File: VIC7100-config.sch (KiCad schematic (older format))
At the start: 42 parts, among them J1 TAG-10PIN, Q1 DMG1013UWQ-7, U13 VIC7100, U2 GD25LQ256DWIGR, U7 STM811RW16F, Y2 ABM8G-25.000MHZ-18-D2Y-T, Y3 ABM8G-27.000MHZ-18-D2Y-T

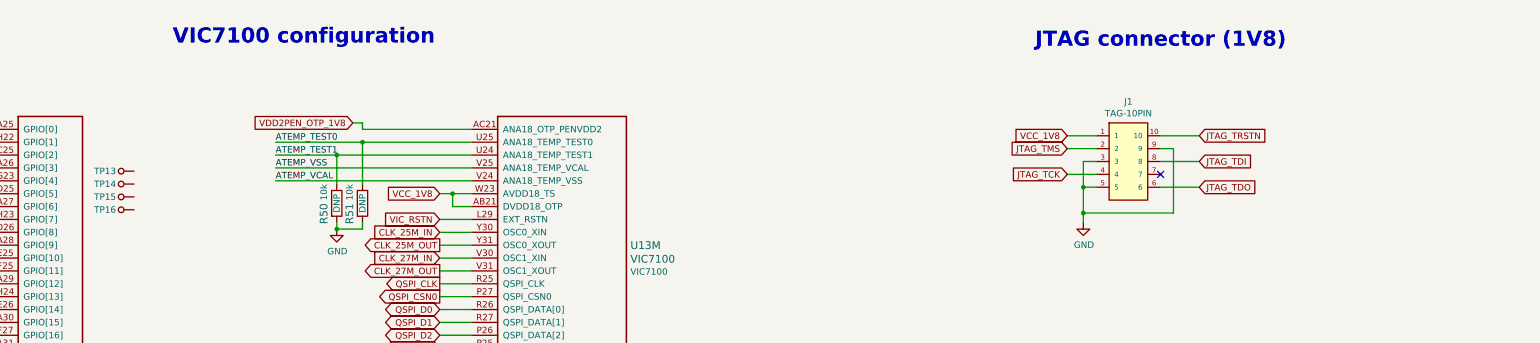
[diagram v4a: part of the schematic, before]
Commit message: Added UART3 testpoints
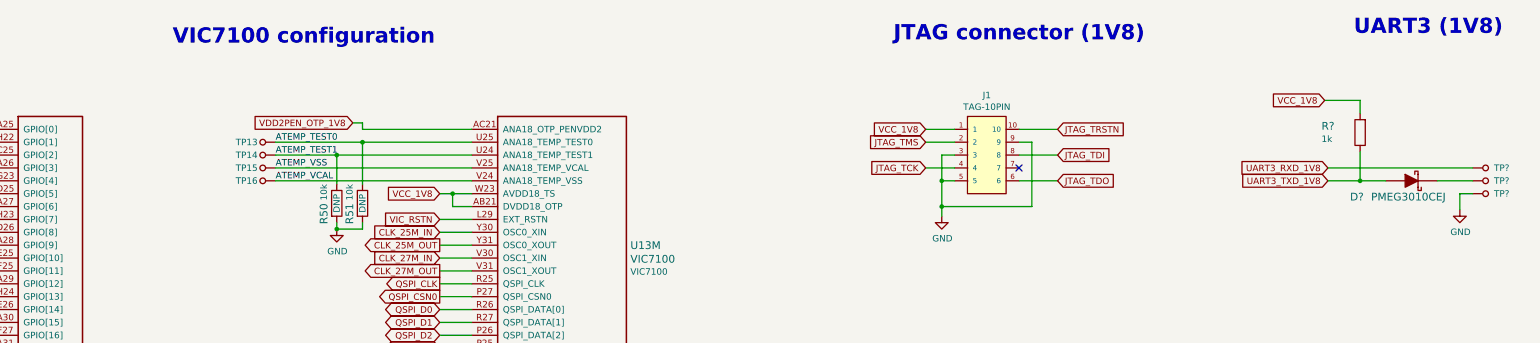
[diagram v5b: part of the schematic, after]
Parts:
- added D?: PMEG3010CEJ, arvsom-footprints:SOD-323F, symbol arvsom:PMEG3010CEJ
- added R?: R_1k_0402, arvsom-footprints:0402-res, symbol arvsom:R_1k_0402
- added TP? (x3): TP_SMD_0_75MM, arvsom-footprints:Testpoint_smd_0_75mm, symbol arvsom:TP_SMD_0_75MM
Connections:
- net ATEMP_TEST0: now also TP13.1
- net ATEMP_TEST1: now also TP14.1
- net ATEMP_VCAL: now also TP16.1
- net ATEMP_VSS: now also TP15.1
- net GND: now also TP?.1
- net UART3_RXD_1V8: now also TP?.1
- net UART3_TXD_1V8: now also D?.A, R?.1
- net VCC_1V8: now also R?.2
- new net: D?.K, TP?.1
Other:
- note added: "UART3 (1V8)"
- moved on the sheet: J1, TP13, TP14, TP15, TP16
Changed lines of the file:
@@
 L arvsom:TP_SMD_0_75MM TP13
 U 1 1 6275FE96
-P 3675 2575
-F 0 "TP13" V 3675 2450 50  0000 C CNN
-F 1 "TP_SMD_0_75MM" H 3675 2475 50  0001 C CNN
-F 2 "arvsom-footprints:Testpoint_smd_0_75mm" H 3875 2775 60  0001 L CNN
-F 3 "" H 3875 2875 60  0001 L CNN
-	1    3675 2575
+P 4775 2350
+F 0 "TP13" V 4775 2225 50  0000 C CNN
+F 1 "TP_SMD_0_75MM" H 4775 2250 50  0001 C CNN
+F 2 "arvsom-footprints:Testpoint_smd_0_75mm" H 4975 2550 60  0001 L CNN
+F 3 "" H 4975 2650 60  0001 L CNN
+	1    4775 2350
 	0    1    1    0
 $EndComp
@@
 L arvsom:TP_SMD_0_75MM TP14
 U 1 1 62760FCD
-P 3675 2675
-F 0 "TP14" V 3675 2550 50  0000 C CNN
-F 1 "TP_SMD_0_75MM" H 3675 2575 50  0001 C CNN
-F 2 "arvsom-footprints:Testpoint_smd_0_75mm" H 3875 2875 60  0001 L CNN
-F 3 "" H 3875 2975 60  0001 L CNN
-	1    3675 2675
+P 4775 2450
+F 0 "TP14" V 4775 2325 50  0000 C CNN
+F 1 "TP_SMD_0_75MM" H 4775 2350 50  0001 C CNN
+F 2 "arvsom-footprints:Testpoint_smd_0_75mm" H 4975 2650 60  0001 L CNN
+F 3 "" H 4975 2750 60  0001 L CNN
+	1    4775 2450
 	0    1    1    0
 $EndComp
@@
 L arvsom:TP_SMD_0_75MM TP15
 U 1 1 62761E35
-P 3675 2775
-F 0 "TP15" V 3675 2650 50  0000 C CNN
-F 1 "TP_SMD_0_75MM" H 3675 2675 50  0001 C CNN
-F 2 "arvsom-footprints:Testpoint_smd_0_75mm" H 3875 2975 60  0001 L CNN
-F 3 "" H 3875 3075 60  0001 L CNN
-	1    3675 2775
+P 4775 2550
+F 0 "TP15" V 4775 2425 50  0000 C CNN
+F 1 "TP_SMD_0_75MM" H 4775 2450 50  0001 C CNN
+F 2 "arvsom-footprints:Testpoint_smd_0_75mm" H 4975 2750 60  0001 L CNN
+F 3 "" H 4975 2850 60  0001 L CNN
+	1    4775 2550
 	0    1    1    0
 $EndComp
@@
 L arvsom:TP_SMD_0_75MM TP16
 U 1 1 62762BE9
-P 3675 2875
-F 0 "TP16" V 3675 2750 50  0000 C CNN
-F 1 "TP_SMD_0_75MM" H 3675 2775 50  0001 C CNN
-F 2 "arvsom-footprints:Testpoint_smd_0_75mm" H 3875 3075 60  0001 L CNN
-F 3 "" H 3875 3175 60  0001 L CNN
-	1    3675 2875
+P 4775 2650
+F 0 "TP16" V 4775 2525 50  0000 C CNN
+F 1 "TP_SMD_0_75MM" H 4775 2550 50  0001 C CNN
+F 2 "arvsom-footprints:Testpoint_smd_0_75mm" H 4975 2850 60  0001 L CNN
+F 3 "" H 4975 2950 60  0001 L CNN
+	1    4775 2650
 	0    1    1    0
 $EndComp
@@
 Text Notes 10975 7500 0    118  ~ 24
 Clock crystals
-Text Notes 10775 1625 0    118  ~ 24
+Text Notes 9675 1575 0    118  ~ 24
 JTAG connector (1V8)
 $Comp
@@
 L arvsom:TAG-10PIN J1
 U 1 1 6099DDAA
-P 11500 2500
-F 0 "J1" H 11500 2965 50  0000 C CNN
-F 1 "TAG-10PIN" H 11500 2874 50  0000 C CNN
-F 2 "arvsom-footprints:Tag-Connect_TC2050-IDC-NL" H 11250 2500 50  0001 L BNN
-F 3 "" H 11500 2500 50  0001 L BNN
-	1    11500 2500
+P 10400 2450
+F 0 "J1" H 10400 2915 50  0000 C CNN
+F 1 "TAG-10PIN" H 10400 2824 50  0000 C CNN
+F 2 "arvsom-footprints:Tag-Connect_TC2050-IDC-NL" H 10150 2450 50  0001 L BNN
+F 3 "" H 10400 2450 50  0001 L BNN
+	1    10400 2450
 	1    0    0    -1
 $EndComp
@@
 Text Notes 5875 5000 0    118  ~ 24
 VIC reset
-Text GLabel 12050 2700 2    50   Input ~ 0
+Text GLabel 10950 2650 2    50   Input ~ 0
 JTAG_TDO
-Text GLabel 11025 2600 0    50   Input ~ 0
+Text GLabel 9925 2550 0    50   Input ~ 0
 JTAG_TCK
-Text GLabel 12050 2500 2    50   Input ~ 0
+Text GLabel 10950 2450 2    50   Input ~ 0
 JTAG_TDI
-Text GLabel 11025 2400 0    50   Input ~ 0
+Text GLabel 9925 2350 0    50   Input ~ 0
 JTAG_TMS
-Text GLabel 12050 2300 2    50   Input ~ 0
+Text GLabel 10950 2250 2    50   Input ~ 0
 JTAG_TRSTN
-Text GLabel 11025 2300 0    50   Input ~ 0
+Text GLabel 9925 2250 0    50   Input ~ 0
 VCC_1V8
 Wire Wire Line
-	11250 2500 11150 2500
-Wire Wire Line
-	11150 2500 11150 2700
-Wire Wire Line
-	11750 2400 11850 2400
-Wire Wire Line
-	11850 2400 11850 2900
-Wire Wire Line
-	11850 2900 11150 2900
-Connection ~ 11150 2900
-Wire Wire Line
-	11150 2900 11150 2975
-NoConn ~ 11750 2600
+	10150 2450 10050 2450
+Wire Wire Line
+	10050 2450 10050 2650
+Wire Wire Line
+	10650 2350 10750 2350
+Wire Wire Line
+	10750 2350 10750 2850
+Wire Wire Line
+	10750 2850 10050 2850
+Connection ~ 10050 2850
+Wire Wire Line
+	10050 2850 10050 2925
+NoConn ~ 10650 2550
 $Comp
 L arvsom:GND #PWR?
 U 1 1 60A2B262
-P 11150 2975
+P 10050 2925
 AR Path="/607858CA/60A2B262" Ref="#PWR?"  Part="1"
 AR Path="/60805CC6/60A2B262" Ref="#PWR0212"  Part="1"
-F 0 "#PWR0212" H 11150 2725 50  0001 C CNN
-F 1 "GND" H 11155 2802 50  0000 C CNN
-F 2 "" H 11150 2975 50  0001 C CNN
-F 3 "" H 11150 2975 50  0001 C CNN
-	1    11150 2975
-	1    0    0    -1
-$EndComp
-Wire Wire Line
-	12050 2700 11750 2700
-Wire Wire Line
-	11750 2500 12050 2500
-Wire Wire Line
-	11750 2300 12050 2300
-Wire Wire Line
-	11025 2300 11250 2300
-Wire Wire Line
-	11025 2400 11250 2400
-Wire Wire Line
-	11025 2600 11250 2600
-Wire Wire Line
-	11250 2700 11150 2700
-Connection ~ 11150 2700
-Wire Wire Line
-	11150 2700 11150 2900
+F 0 "#PWR0212" H 10050 2675 50  0001 C CNN
+F 1 "GND" H 10055 2752 50  0000 C CNN
+F 2 "" H 10050 2925 50  0001 C CNN
+F 3 "" H 10050 2925 50  0001 C CNN
+	1    10050 2925
+	1    0    0    -1
+$EndComp
+Wire Wire Line
+	10950 2650 10650 2650
+Wire Wire Line
+	10650 2450 10950 2450
+Wire Wire Line
+	10650 2250 10950 2250
+Wire Wire Line
+	9925 2250 10150 2250
+Wire Wire Line
+	9925 2350 10150 2350
+Wire Wire Line
+	9925 2550 10150 2550
+Wire Wire Line
+	10150 2650 10050 2650
+Connection ~ 10050 2650
+Wire Wire Line
+	10050 2650 10050 2850
 Wire Wire Line
 	10225 6125 10150 6125
@@
 	1    0    0    -1
 $EndComp
+Text GLabel 13050 2550 0    50   Input ~ 0
+UART3_RXD_1V8
+Text GLabel 13050 2650 0    50   Input ~ 0
+UART3_TXD_1V8
+Text GLabel 13025 2025 0    50   Input ~ 0
+VCC_1V8
+$Comp
+L arvsom:PMEG3010CEJ D?
+U 1 1 609A2E9D
+P 13700 2650
+AR Path="/60751C8D/609A2E9D" Ref="D?"  Part="1"
+AR Path="/60805CC6/609A2E9D" Ref="D?"  Part="1"
+F 0 "D?" H 13275 2525 60  0000 C CNN
+F 1 "PMEG3010CEJ" H 13675 2525 60  0000 C CNN
+F 2 "arvsom-footprints:SOD-323F" H 13900 2850 60  0001 L CNN
+F 3 "https://assets.nexperia.com/documents/data-sheet/PMEG3010CEH_PMEG3010CEJ.pdf" H 13900 2950 60  0001 L CNN
+F 4 "PMEG3010CEJ" H 13900 3150 60  0001 L CNN "MPN"
+F 5 "Nexperia" H 13900 3750 60  0001 L CNN "Manufacturer"
+	1    13700 2650
+	1    0    0    -1
+$EndComp
+$Comp
+L arvsom:R_1k_0402 R?
+U 1 1 609A653A
+P 13300 2275
+AR Path="/60751C8D/609A653A" Ref="R?"  Part="1"
+AR Path="/60805CC6/609A653A" Ref="R?"  Part="1"
+F 0 "R?" V 13350 2575 60  0000 R CNN
+F 1 "R_1k_0402" H 13300 2125 60  0001 C CNN
+F 2 "arvsom-footprints:0402-res" H 13500 2475 60  0001 L CNN
+F 3 "" H 13300 2275 50  0001 C CNN
+F 4 "BOURNS" H 13500 2675 60  0001 L CNN "Manufacturer"
+F 5 "CR0402-FX-1001GLF" H 13500 2575 60  0001 L CNN "MPN"
+F 6 "1k" V 13250 2575 50  0000 R CNN "Val"
+	1    13300 2275
+	0    -1   -1   0
+$EndComp
+Wire Wire Line
+	13025 2025 13300 2025
+Wire Wire Line
+	13300 2025 13300 2125
+Wire Wire Line
+	13050 2550 14175 2550
+Wire Wire Line
+	13300 2425 13300 2650
+Wire Wire Line
+	13050 2650 13300 2650
+Connection ~ 13300 2650
+Wire Wire Line
+	13300 2650 13500 2650
+Wire Wire Line
+	13900 2650 14175 2650
+Text Notes 13250 1525 0    118  ~ 24
+UART3 (1V8)
+$Comp
+L arvsom:TP_SMD_0_75MM TP?
+U 1 1 60A17308
+P 14275 2750
+F 0 "TP?" V 14275 2625 50  0000 C CNN
+F 1 "TP_SMD_0_75MM" H 14275 2650 50  0001 C CNN
+F 2 "arvsom-footprints:Testpoint_smd_0_75mm" H 14475 2950 60  0001 L CNN
+F 3 "" H 14475 3050 60  0001 L CNN
+	1    14275 2750
+	0    -1   -1   0
+$EndComp
+$Comp
+L arvsom:TP_SMD_0_75MM TP?
+U 1 1 60A1730E
+P 14275 2650
+F 0 "TP?" V 14275 2525 50  0000 C CNN
+F 1 "TP_SMD_0_75MM" H 14275 2550 50  0001 C CNN
+F 2 "arvsom-footprints:Testpoint_smd_0_75mm" H 14475 2850 60  0001 L CNN
+F 3 "" H 14475 2950 60  0001 L CNN
+	1    14275 2650
+	0    -1   -1   0
+$EndComp
+$Comp
+L arvsom:TP_SMD_0_75MM TP?
+U 1 1 60A17314
+P 14275 2550
+F 0 "TP?" V 14275 2425 50  0000 C CNN
+F 1 "TP_SMD_0_75MM" H 14275 2450 50  0001 C CNN
+F 2 "arvsom-footprints:Testpoint_smd_0_75mm" H 14475 2750 60  0001 L CNN
+F 3 "" H 14475 2850 60  0001 L CNN
+	1    14275 2550
+	0    -1   -1   0
+$EndComp
+Wire Wire Line
+	14175 2750 14075 2750
+Wire Wire Line
+	14075 2750 14075 2875
+$Comp
+L arvsom:GND #PWR?
+U 1 1 60A328F3
+P 14075 2875
+AR Path="/607858CA/60A328F3" Ref="#PWR?"  Part="1"
+AR Path="/60805CC6/60A328F3" Ref="#PWR?"  Part="1"
+F 0 "#PWR?" H 14075 2625 50  0001 C CNN
+F 1 "GND" H 14080 2702 50  0000 C CNN
+F 2 "" H 14075 2875 50  0001 C CNN
+F 3 "" H 14075 2875 50  0001 C CNN
+	1    14075 2875
+	1    0    0    -1
+$EndComp

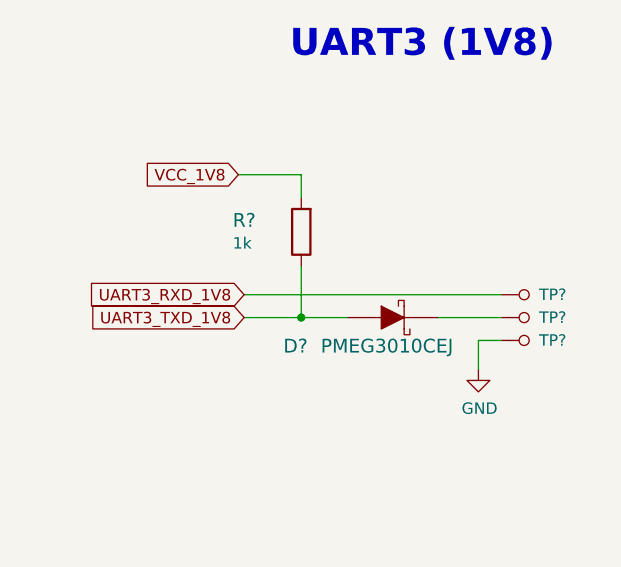
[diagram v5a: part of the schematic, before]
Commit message: Fixed two DDR pinout errors
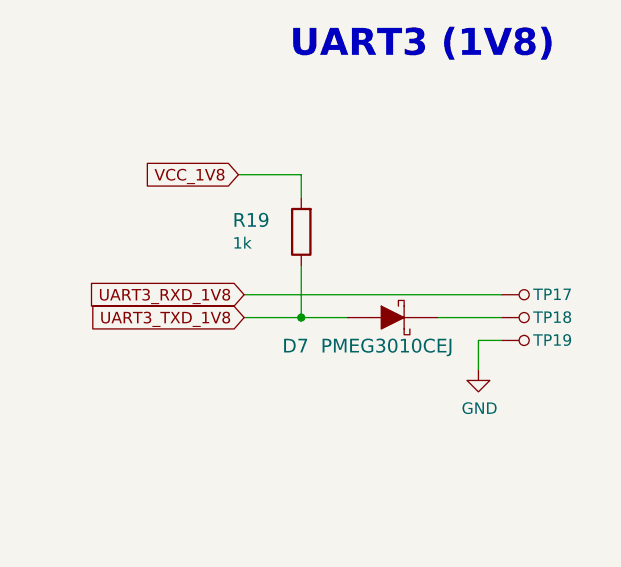
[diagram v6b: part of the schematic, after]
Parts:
- gave numbers to parts that had none: 5
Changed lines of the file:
@@
 P 13700 2650
 AR Path="/60751C8D/609A2E9D" Ref="D?"  Part="1"
-AR Path="/60805CC6/609A2E9D" Ref="D?"  Part="1"
-F 0 "D?" H 13275 2525 60  0000 C CNN
+AR Path="/60805CC6/609A2E9D" Ref="D7"  Part="1"
+F 0 "D7" H 13275 2525 60  0000 C CNN
 F 1 "PMEG3010CEJ" H 13675 2525 60  0000 C CNN
 F 2 "arvsom-footprints:SOD-323F" H 13900 2850 60  0001 L CNN
@@
 P 13300 2275
 AR Path="/60751C8D/609A653A" Ref="R?"  Part="1"
-AR Path="/60805CC6/609A653A" Ref="R?"  Part="1"
-F 0 "R?" V 13350 2575 60  0000 R CNN
+AR Path="/60805CC6/609A653A" Ref="R19"  Part="1"
+F 0 "R19" V 13350 2575 60  0000 R CNN
 F 1 "R_1k_0402" H 13300 2125 60  0001 C CNN
 F 2 "arvsom-footprints:0402-res" H 13500 2475 60  0001 L CNN
@@
 UART3 (1V8)
 $Comp
-L arvsom:TP_SMD_0_75MM TP?
+L arvsom:TP_SMD_0_75MM TP19
 U 1 1 60A17308
 P 14275 2750
-F 0 "TP?" V 14275 2625 50  0000 C CNN
+F 0 "TP19" V 14275 2625 50  0000 C CNN
 F 1 "TP_SMD_0_75MM" H 14275 2650 50  0001 C CNN
 F 2 "arvsom-footprints:Testpoint_smd_0_75mm" H 14475 2950 60  0001 L CNN
@@
 $EndComp
 $Comp
-L arvsom:TP_SMD_0_75MM TP?
+L arvsom:TP_SMD_0_75MM TP18
 U 1 1 60A1730E
 P 14275 2650
-F 0 "TP?" V 14275 2525 50  0000 C CNN
+F 0 "TP18" V 14275 2525 50  0000 C CNN
 F 1 "TP_SMD_0_75MM" H 14275 2550 50  0001 C CNN
 F 2 "arvsom-footprints:Testpoint_smd_0_75mm" H 14475 2850 60  0001 L CNN
@@
 $EndComp
 $Comp
-L arvsom:TP_SMD_0_75MM TP?
+L arvsom:TP_SMD_0_75MM TP17
 U 1 1 60A17314
 P 14275 2550
-F 0 "TP?" V 14275 2425 50  0000 C CNN
+F 0 "TP17" V 14275 2425 50  0000 C CNN
 F 1 "TP_SMD_0_75MM" H 14275 2450 50  0001 C CNN
 F 2 "arvsom-footprints:Testpoint_smd_0_75mm" H 14475 2750 60  0001 L CNN
@@
 P 14075 2875
 AR Path="/607858CA/60A328F3" Ref="#PWR?"  Part="1"
-AR Path="/60805CC6/60A328F3" Ref="#PWR?"  Part="1"
-F 0 "#PWR?" H 14075 2625 50  0001 C CNN
+AR Path="/60805CC6/60A328F3" Ref="#PWR0265"  Part="1"
+F 0 "#PWR0265" H 14075 2625 50  0001 C CNN
 F 1 "GND" H 14080 2702 50  0000 C CNN
 F 2 "" H 14075 2875 50  0001 C CNN

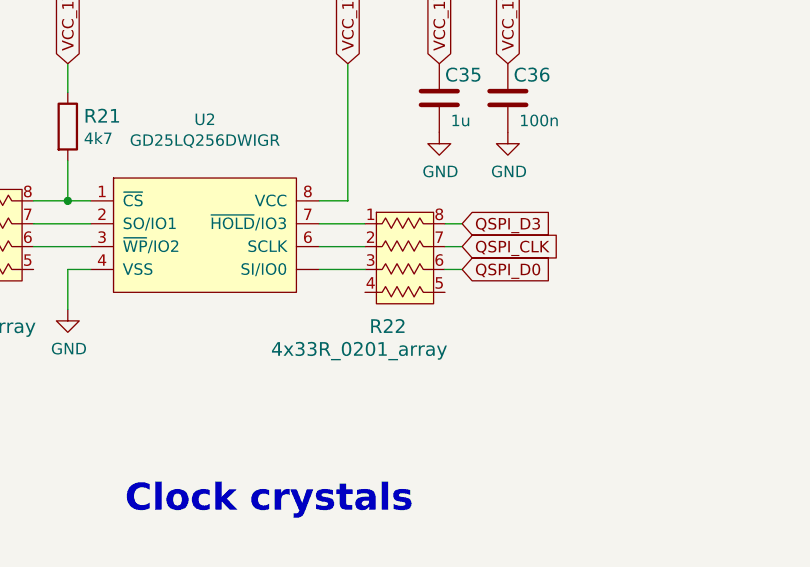
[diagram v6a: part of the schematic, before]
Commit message: Updated component placement - HDMI IC passives, QSPI, 5V8 buck placed
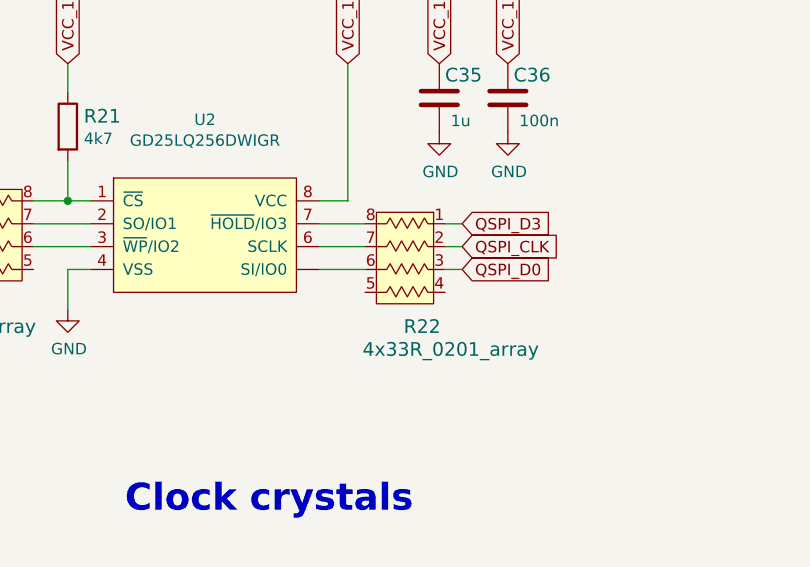
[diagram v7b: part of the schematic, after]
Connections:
- net QSPI_CLK: now also R22.2; no longer R22.7
- net QSPI_D0: now also R22.3; no longer R22.6
- net QSPI_D3: now also R22.1; no longer R22.8
- net at U2.7 (~HOLD~/IO3): now also R22.8; no longer R22.1
- net at U2.6 (SCLK): now also R22.7; no longer R22.2
- net at U2.~ (SI/IO0): now also R22.6; no longer R22.3
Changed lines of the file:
@@
 L arvsom:4x33R_0201_array R22
 U 1 1 609DE671
-P 12225 6625
-F 0 "R22" H 12125 6575 60  0000 C CNN
-F 1 "4x33R_0201_array" H 12000 6475 60  0000 C CNN
-F 2 "arvsom-footprints:EXB18V" H 12025 7375 60  0001 L CNN
-F 3 "http://industrial.panasonic.com/cdbs/www-data/pdf/AOC0000/AOC0000C14.pdf" H 12025 7375 60  0001 L CNN
-F 4 "EXB-18V330JX" H 12025 7575 60  0001 L CNN "MPN"
-F 5 "Panasonic" H 12025 7475 60  0001 L CNN "Manufacturer"
-	1    12225 6625
-	1    0    0    -1
+P 12175 6625
+F 0 "R22" H 12075 6575 60  0000 C CNN
+F 1 "4x33R_0201_array" H 11950 6475 60  0000 C CNN
+F 2 "arvsom-footprints:EXB18V" H 11975 7375 60  0001 L CNN
+F 3 "http://industrial.panasonic.com/cdbs/www-data/pdf/AOC0000/AOC0000C14.pdf" H 11975 7375 60  0001 L CNN
+F 4 "EXB-18V330JX" H 11975 7575 60  0001 L CNN "MPN"
+F 5 "Panasonic" H 11975 7475 60  0001 L CNN "Manufacturer"
+	1    12175 6625
+	-1   0    0    -1
 $EndComp
 Wire Wire Line

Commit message: Finished component placement
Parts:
- removed R109, R110, R111, R112, R113, R114, R115, R116, R50, R51, R52, R53, R54: R_10k_0402, arvsom-footprints:0402-res, symbol arvsom:R_10k_0402
- added R109, R110, R111, R112, R113, R114, R115, R116, R50, R51, R52, R53, R54: R_10k_0201, arvsom-footprints:0201-res, symbol arvsom:R_10k_0201
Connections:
- wire segments 186 -> 188
